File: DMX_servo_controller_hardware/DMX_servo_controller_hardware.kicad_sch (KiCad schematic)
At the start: 67 parts, among them J1 Power connector, J10 Conn_01x03, J11 Conn_01x03, J12 Conn_01x03, J2 XLR, J3 Display, J4 Rotary encoder, J5 Conn_01x03, J6 Conn_01x03, J7 Conn_01x03, J8 Conn_01x03, J9 Conn_01x03, Q1 BSS138, Q2 BSS138, SW1 Reset, U1 PCA9685PW, U2 SN65HVD11HD, U3 6N137, U4 Pico

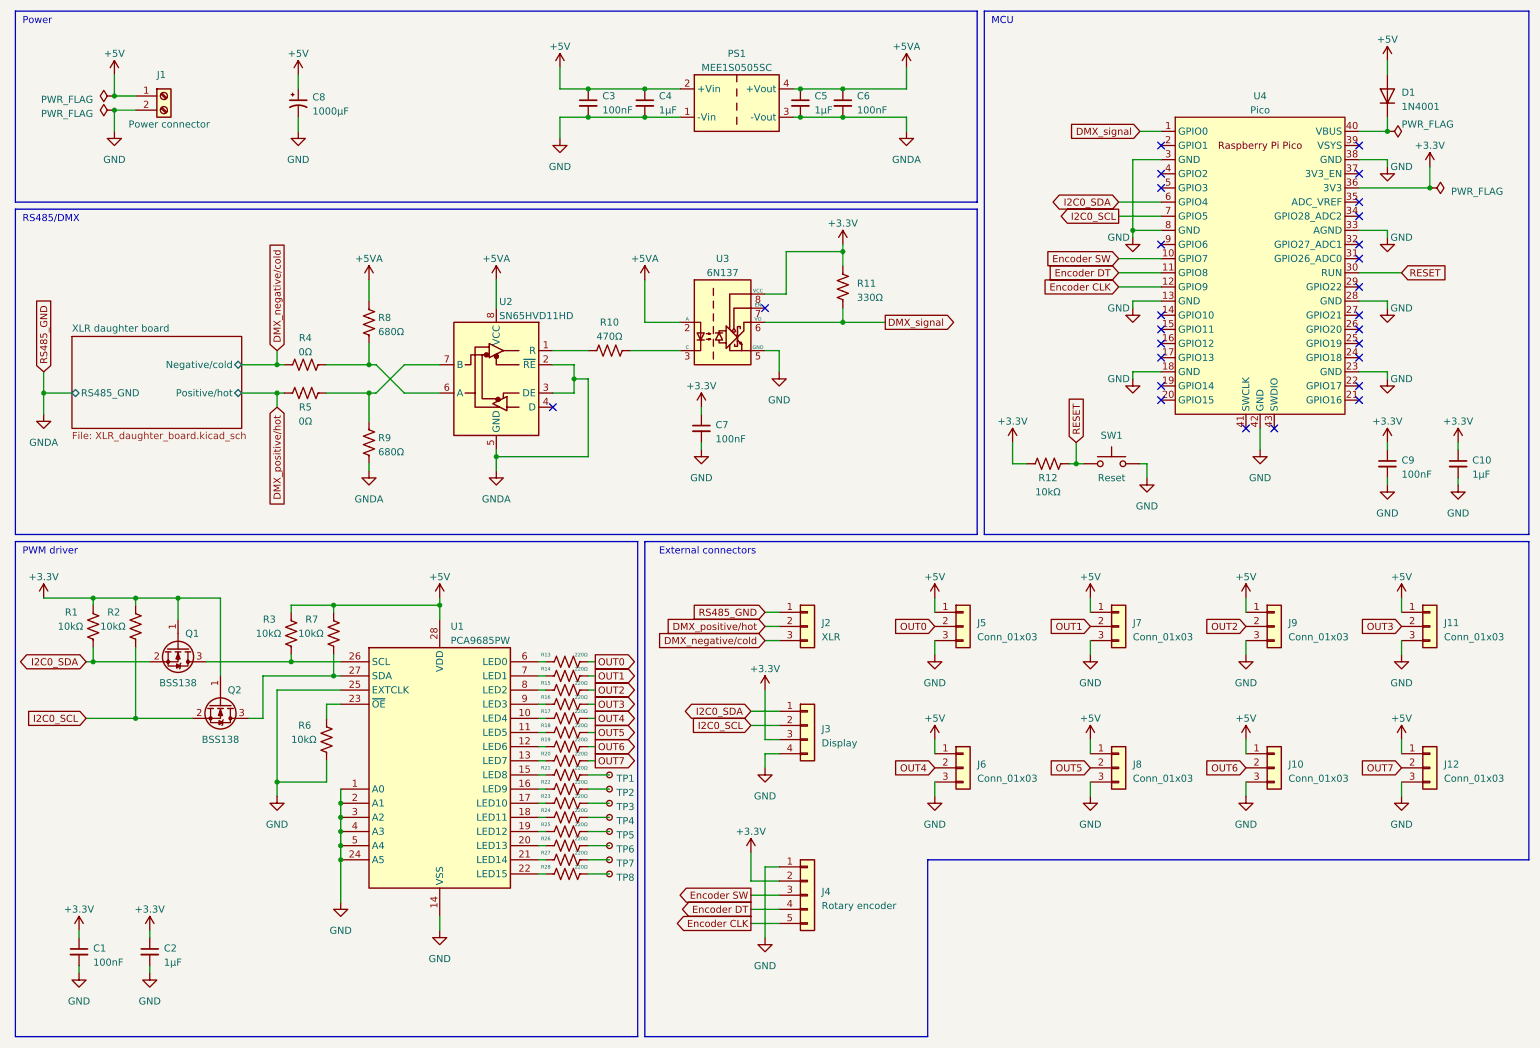
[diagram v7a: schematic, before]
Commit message: Changes schematic to have only header to plug the panel mounted XLR3 connectors
We will use panel mounted XLR connector, so we don't need the daughter
board and the PCB XLR connectors anymore. Instead, the external ones
will connect to the PCB via 2 JST headers.
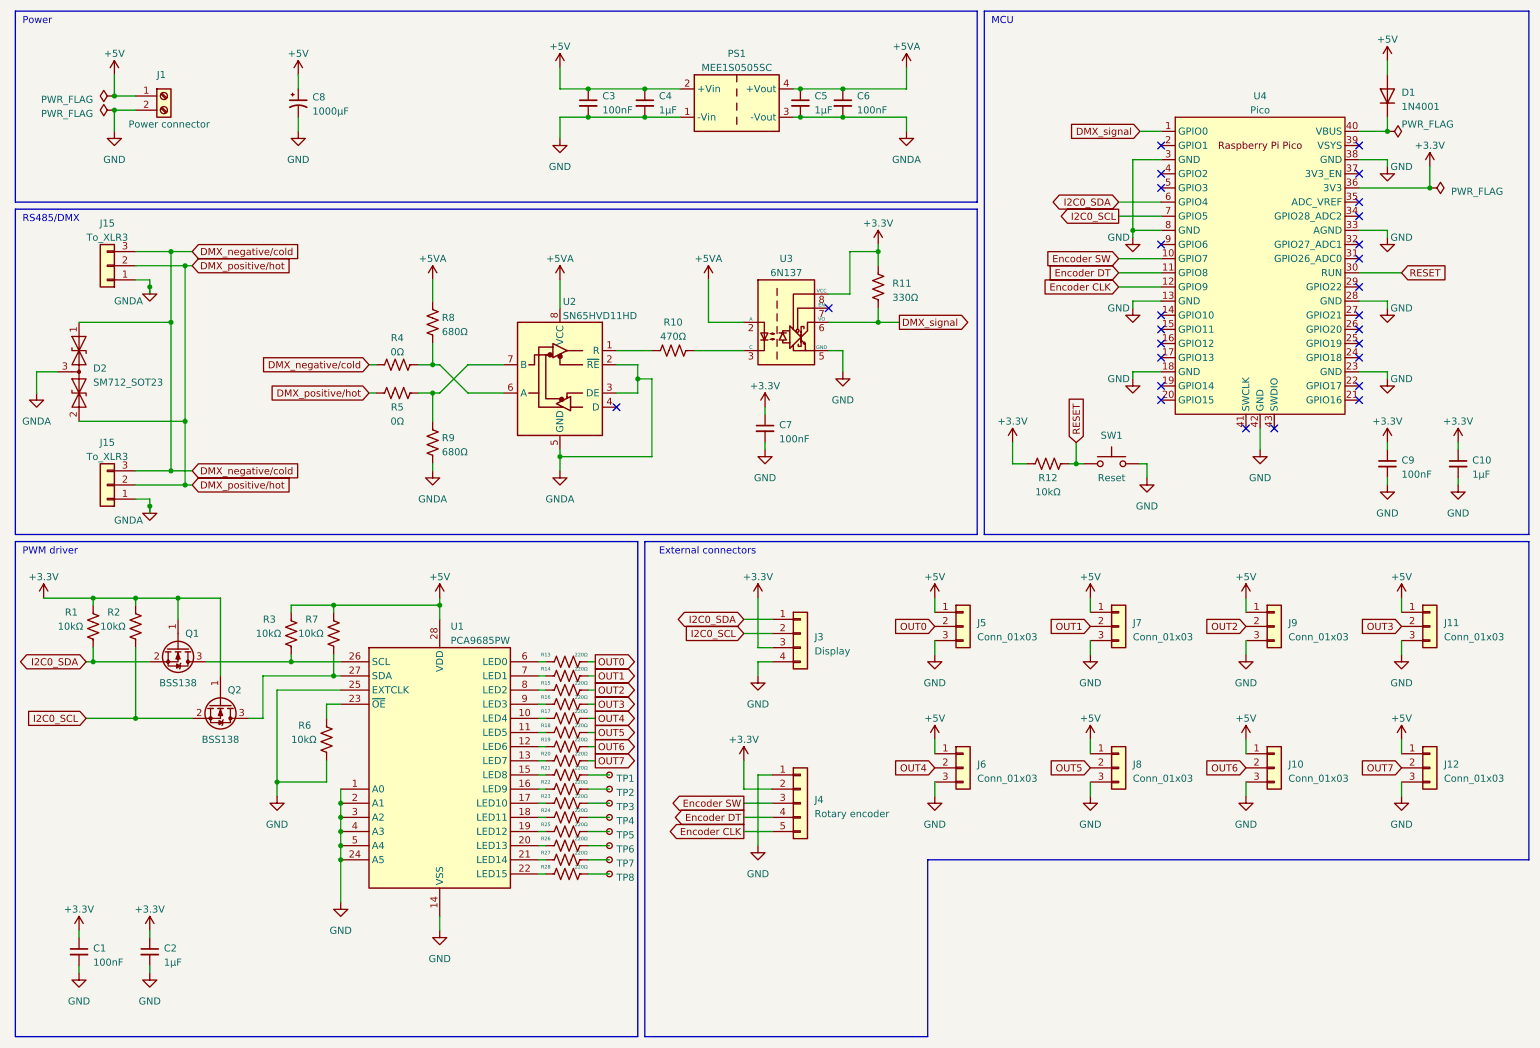
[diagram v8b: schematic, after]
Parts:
- removed J2: XLR, symbol Connector_Generic:Conn_01x03
- added D2: SM712_SOT23, Package_TO_SOT_SMD:SOT-23, symbol Diode:SM712_SOT23
- added J15 (x2): To_XLR3, Connector_JST:JST_XH_B3B-XH-AM_1x03_P2.50mm_Vertical, symbol Connector_Generic:Conn_01x03
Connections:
- net DMX_negative/cold: now also D2.1 (A1), J15.3 (Pin_3), J15.3 (Pin_3)
- net DMX_positive/hot: now also D2.2 (A2), J15.2 (Pin_2), J15.2 (Pin_2)
- net GNDA: now also D2.3 (common), J15.1 (Pin_1), J15.1 (Pin_1)
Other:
- removed sheet XLR daughter board
- moved on the sheet: C7, J3, J4, R10, R11, R4, R5, R8, R9, U2, U3
